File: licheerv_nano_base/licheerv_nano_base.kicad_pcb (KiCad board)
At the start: 2 copper layers, 186 x 50 mm, 112 parts, among them J1 USB STM32, J10 Valve, J11 ETH_IN, J12 ETH_OUT, J13 Compressor, J14 DebugUART, J15 Weight, J16 Malibotti, J17 Robot, J18 SWDBG, J19 IO, J2 Barrel_Jack_Switch, J3 TOF1, J4 TOF1, J5 TOF1, J6 TOF1, J7 STEP1, J8 STEP2, J9 Conveyor, Q1 BC807, Q2 IRLML6344, Q3 IRLML6344, Q4 IRLML6344, U1 TPS54202DDC, U2 STM32G431RBTx, U3 HX711, U5 TMC2209, U6 TMC2209

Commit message: Initial commit lichee_rv_nano_base pcb
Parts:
- added FID2: Fiducial, liebler_DRAWINGS:barrel_jack_positive_polarity, F.Cu at (155.9, 68.8)
- added R11: 10k, Resistor_SMD:R_0201_0603Metric, B.Cu at (168.2, 59.2)
- added U4: DCDC_MP2315, liebler_MODULES:DCDC_MP2315, F.Cu at (68.5, 77.8)
- C5, C7: footprint Capacitor_SMD:C_0603_1608Metric -> Capacitor_SMD:C_0805_2012Metric
- C8: value 1u -> 2u2
- J2: value Barrel_Jack_Switch -> DC IN
- J3: value TOF1 -> TOF3
- J4: value TOF1 -> TOF2
- L1: footprint liebler_PASSIVES:L_0630 -> Inductor_SMD:L_Abracon_ASPI-0630LR
- LS2: value Speaker_withoutTerminals -> Speaker
- Q1: footprint Package_TO_SOT_SMD:SOT-23_Handsoldering -> liebler_SEMICONDUCTORS:SOT-23_smaller
- R2: footprint Resistor_SMD:R_0201_0603Metric -> Resistor_SMD:R_0402_1005Metric
- R5, R6, R7: footprint Resistor_SMD:R_0805_2012Metric_Pad1.20x1.40mm_HandSolder -> Resistor_SMD:R_0402_1005Metric
- R8: value 20k -> 10k; footprint Resistor_SMD:R_0805_2012Metric_Pad1.20x1.40mm_HandSolder -> Resistor_SMD:R_0201_0603Metric
- TP1: value Stepper_UART -> StepperUART
- U7: value ~ -> PoE->24V
- moved J11 16.6 mm to (38.7, 64.6)
- moved C7 16.5 mm to (85.4, 73.0)
- moved J12 16.5 mm to (55.3, 64.6)
- moved C5 16.2 mm to (83.4, 73.0)
- moved J16 12.6 mm to (77.2, 91.9)
- moved J17 12.6 mm to (64.5, 91.9)
- moved L1 10.00 mm to (78.0, 69.2), turned to 180 degrees
- moved Q2 9.55 mm to (58.7, 61.5)
- moved R4 7.01 mm to (66.7, 66.6), turned to -90 degrees
- moved C3 6.80 mm to (67.9, 67.2), turned to 90 degrees
- moved R3 6.12 mm to (66.7, 68.3), turned to -90 degrees
- moved R2 6.03 mm to (67.2, 70.1), turned to 90 degrees
- moved L2 5.54 mm to (161.3, 57.0)
- moved C1 5.20 mm to (72.6, 71.9), turned to 180 degrees
- moved R7 4.95 mm to (168.8, 55.7)
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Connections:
- net Net-(J14-Pin_2) renamed /RX
- net Net-(J14-Pin_3) renamed /TX
- J3 pad 1: i1c -> i3c
- J3 pad 2: i1d -> i3d
- J3 pad 3: INT_TOF1 -> INT_TOF3
- J4 pad 1: i2c -> i1c
- J4 pad 2: i2d -> i1d
- J4 pad 3: INT_TOF2 -> INT_TOF1
- J5 pad 1: i3c -> i2c
- J5 pad 2: i3d -> i2d
- J5 pad 3: INT_TOF3 -> INT_TOF2
- R8 pad 2: Net-(U3-VFB) -> Net-(R11-Pad1)
- U2 pad 12: INT_TOF3 -> INT_TOF2
- U2 pad 13: INT_TOF2 -> INT_TOF1
- U2 pad 22: i2c -> i1c
- U2 pad 40: i3c -> i2c
- U2 pad 41: i3d -> i2d
- U2 pad 5: i2d -> i1d
- U2 pad 51: i1c -> i3c
- U2 pad 60: i1d -> i3d
- U2 pad 62: INT_TOF1 -> INT_TOF3
- U8 pad 23: MALIBOTTI_RXD -> ROBOT_RXD
- U8 pad 25: MALIBOTTI_TXD -> ROBOT_TXD
- U8 pad 27: ROBOT_RXD -> MALIBOTTI_RXD
- U8 pad 28: ROBOT_TXD -> MALIBOTTI_TXD
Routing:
- net +3V3: track 282.1 -> 341.9 mm, vias 9 -> 10
- net +5V: track 100.5 -> 83.6 mm, vias 1 -> 2
- net INT_TOF2: track 23.8 -> 6.99 mm
- net ROBOT_RXD: track 9.37 -> 25.9 mm
- net 5-24V: track 221.3 -> 236.7 mm, vias 9 -> 20
- net INT_TOF3: track 6.99 -> 21.8 mm
- net ROBOT_TXD: track 6.80 -> 21.1 mm
- net MALIBOTTI_RXD: track 24.0 -> 9.76 mm
- net GND: track 73.1 -> 86.8 mm, vias 12 -> 172
- net +9V: track 0.00 -> 12.2 mm
- net MALIBOTTI_TXD: track 19.3 -> 7.38 mm
- net INT_RGB: track 55.4 -> 43.5 mm, vias 0 -> 1
- net i2d: track 29.8 -> 20.2 mm
- net i1d: track 20.3 -> 29.8 mm
- net +48V: track 22.3 -> 14.8 mm
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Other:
- board text added: "+ -"
- board text added: "3V3"
- board text added: "5V"
- board text added: "9V"
- board text added: "A+"
- board text added: "A-"
- board text added: "A1"
- board text added: "A2"
- board text added: "B1"
- board text added: "B2"
- board text added: "Compr"
- board text added: "Conv"
- board text added: "E+"
- board text added: "E-"
- board text added: "GND"
- board text added: "I1C"
- board text added: "I1D"
- board text added: "I2C"
- board text added: "I2D"
- board text added: "I3C"
- board text added: "I3D"
- board text added: "IO1"
- board text added: "IO2"
- board text added: "IO3"
- board text added: "IO4"
- board text added: "IRQ"
- board text added: "IRQ1"
- board text added: "IRQ2"
- board text added: "IRQ3"
- board text added: "Malibotti"
- board text added: "RX"
- board text added: "RXD"
- board text added: "Robot"
- board text added: "SCL"
- board text added: "SDA"
- board text added: "Stepper1"
- board text added: "Stepper2"
- board text added: "TX"
- board text added: "TXD"
- board text added: "USB PD"
- board text added: "Valve"
- board text added: "Weightcell"

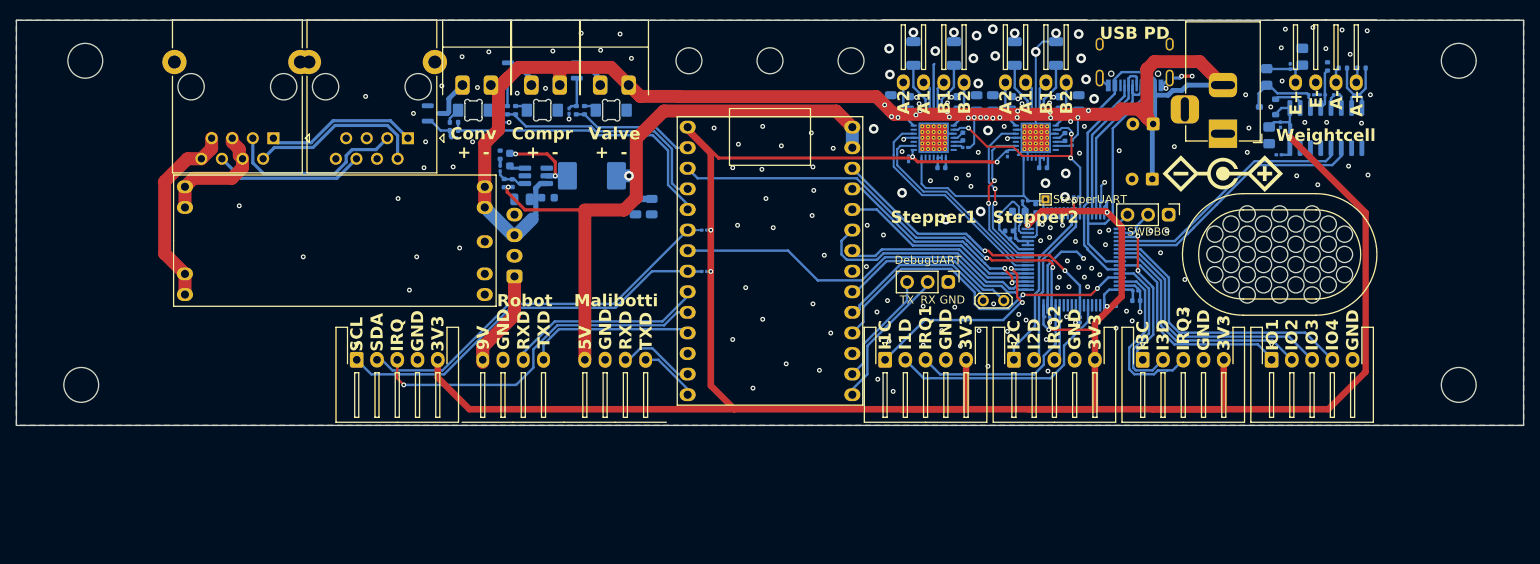
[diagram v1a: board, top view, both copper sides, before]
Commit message: lichee_rv_nano aka radxa zero 3e as ordered @ jlcpcb
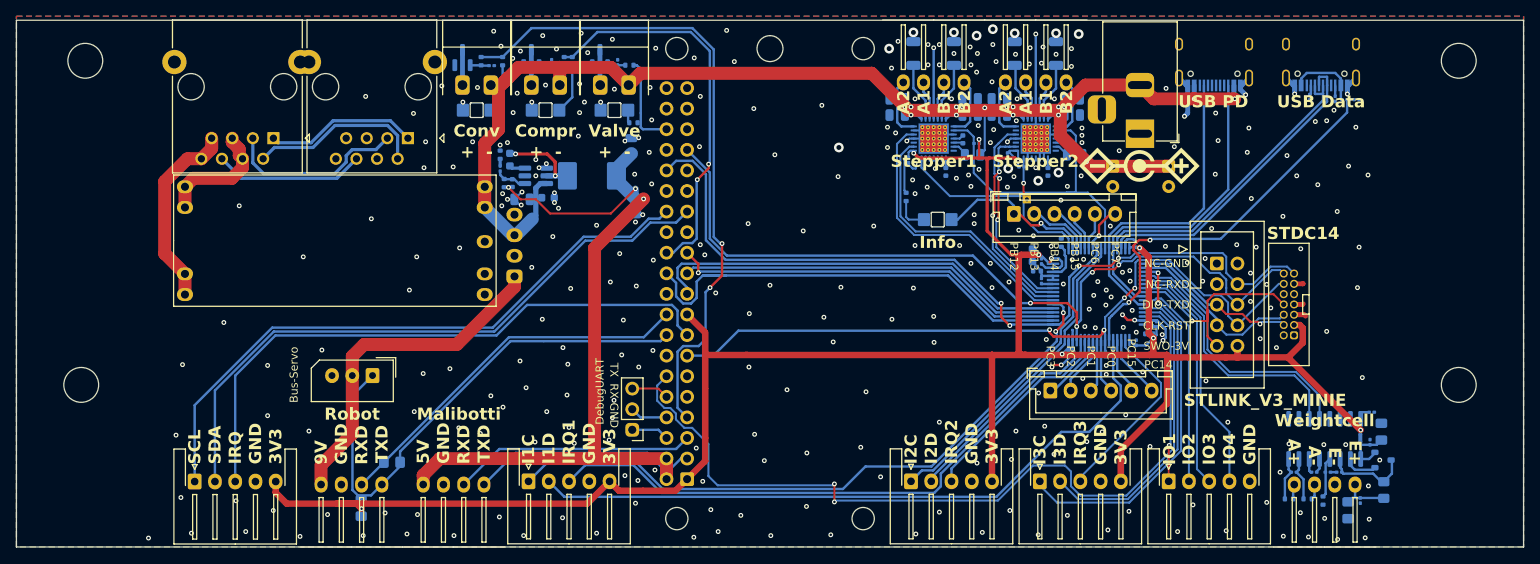
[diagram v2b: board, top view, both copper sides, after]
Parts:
- removed H5, H7: MountingHole, MountingHole:MountingHole_3.2mm_M3
- removed LS1: Speaker, TestPoint:TestPoint_2Pads_Pitch2.54mm_Drill0.8mm
- removed LS2: Speaker, liebler_MECH:SPEAKER_2415
- removed R12, R14: 4k7, Resistor_SMD:R_0201_0603Metric
- removed U8: ~, liebler_MODULES:LicheeRV_Nano
- added D4: Info, liebler_OPTO:LED_1206_3216Metric_ReverseMount, B.Cu at (120.7, 74.6)
- added J20: Bus-Servo, Connector_Molex:Molex_SPOX_5267-03A_1x03_P2.50mm_Vertical, F.Cu at (51.0, 93.8)
- added J21: STDC14, liebler_CONN:IDC_2x07_P1.27mm_Vertical, F.Cu at (164.0, 85.1)
- added J22: USB STM32, liebler_CONN:USB_C_Receptacle_HRO_TYPE-C-31-M-12_smaller, B.Cu at (168.0, 54.0)
- added J23: IO, Connector_JST:JST_XH_B6B-XH-A_1x06_P2.50mm_Vertical, F.Cu at (130.1, 73.9)
- added J24: IO, Connector_JST:JST_XH_B6B-XH-A_1x06_P2.50mm_Vertical, F.Cu at (134.6, 95.7)
- added R13: 5k1, Resistor_SMD:R_0201_0603Metric, B.Cu at (166.6, 59.5)
- added R28: 5k1, Resistor_SMD:R_0201_0603Metric, B.Cu at (169.8, 59.7)
- added R29: 10k, Resistor_SMD:R_0201_0603Metric, B.Cu at (170.9, 59.8)
- added R30: 10k, Resistor_SMD:R_0201_0603Metric, B.Cu at (172.4, 59.8)
- added R31: 1k, Resistor_SMD:R_0402_1005Metric, B.Cu at (116.8, 71.8)
- added R76: 10k, Resistor_SMD:R_0805_2012Metric_Pad1.20x1.40mm_HandSolder, B.Cu at (49.5, 110.2)
- added R77: 1k, Resistor_SMD:R_0805_2012Metric_Pad1.20x1.40mm_HandSolder, B.Cu at (53.4, 104.5)
- added X1: Radxa Zero 3E, liebler_MODULES:Radxa Zero 3E, B.Cu at (88.5, 82.5)
- C25, C26: footprint Capacitor_SMD:C_0201_0603Metric -> Capacitor_SMD:C_0805_2012Metric
- C29, C30, C42, C43: footprint Capacitor_SMD:C_0603_1608Metric -> Capacitor_SMD:C_0805_2012Metric
- J18: value SWDBG -> STLINK_V3_MINIE; footprint liebler_CONN:PinHeader_1x03_P2.54mm_Vertical_smallerCourtyard -> Connector_IDC:IDC-Header_2x05_P2.54mm_Vertical
- TP1: moved to B.Cu
- moved C10 56.3 mm to (171.3, 110.5), turned to -90 degrees
- moved C6 54.3 mm to (172.8, 109.3), turned to -90 degrees
- moved R5 53.9 mm to (164.1, 109.1), turned to 0 degrees
- moved R7 53.6 mm to (168.2, 109.3), turned to -90 degrees
- moved R6 53.4 mm to (166.3, 109.1), turned to 0 degrees
- moved L2 53.0 mm to (175.8, 108.0), turned to 90 degrees
- moved J15 50.2 mm to (164.7, 107.3), turned to 0 degrees
- moved C11 47.2 mm to (164.7, 105.8), turned to 0 degrees
- moved R8 46.7 mm to (170.2, 105.8), turned to 180 degrees
- moved C13 46.7 mm to (167.2, 105.8), turned to 0 degrees
- moved R11 46.6 mm to (168.8, 105.8), turned to 180 degrees
- moved J4 46.5 mm to (70.2, 106.9)
- moved Q1 45.8 mm to (175.7, 104.3), turned to 0 degrees
- moved J14 43.1 mm to (83.0, 100.5), turned to 180 degrees
- moved C20 40.7 mm to (174.1, 102.1), turned to 90 degrees
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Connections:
- net /BOOT renamed /psu/BOOT
- net /FB renamed /psu/FB
- net /SW renamed /psu/SW
- J1 pad A6: USBPD_D+ -> unconnected-(J1-D+-PadA6)
- J1 pad A7: USBPD_D- -> unconnected-(J1-D--PadA7)
- J1 pad B6: USBPD_D+ -> unconnected-(J1-D+-PadB6)
- J1 pad B7: USBPD_D- -> unconnected-(J1-D--PadB7)
- J18 pad 1: GND -> unconnected-(J18-Pin_1-Pad1)
- J18 pad 2: SWCLK -> GND
- J18 pad 3: SWDIO -> unconnected-(J18-Pin_3-Pad3)
- U2 pad 2: unconnected-(U2-PC13-Pad2) -> INT_TOF3
- U2 pad 3: unconnected-(U2-PC14-Pad3) -> PC14
- U2 pad 4: unconnected-(U2-PC15-Pad4) -> PC15
- U2 pad 56: IO2 -> SWO
- U2 pad 58: IO1 -> IO2
- U2 pad 6: unconnected-(U2-PF1-Pad6) -> USB_VSENSE
- U2 pad 62: INT_TOF3 -> IO1
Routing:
- net STM32_BOOT: track 42.1 -> 103.0 mm
- net 5-24V: track 236.7 -> 177.1 mm, vias 20 -> 16
- net STM32BOOT_RXD: track 46.6 -> 102.7 mm, vias 0 -> 4
- net i1c: track 26.8 -> 81.7 mm
- net i1d: track 29.8 -> 84.1 mm
- net STM32_RESET: track 38.0 -> 91.2 mm, vias 2 -> 4
- net INT_TOF1: track 23.8 -> 75.0 mm
- net USB_VSENSE: track 0.00 -> 49.4 mm, vias 0 -> 2
- net STM32BOOT_TXD: track 55.1 -> 102.0 mm, vias 2 -> 4
- net +3V3: track 341.9 -> 295.6 mm, vias 10 -> 9
- net Conveyor_PWM: track 36.2 -> 81.1 mm, vias 0 -> 2
- net ROBOT_TXD: track 21.1 -> 63.4 mm
- net INT_RGB: track 43.5 -> 75.1 mm, vias 1 -> 0
- net SDA: track 47.8 -> 78.7 mm
- net +9V: track 12.2 -> 42.3 mm
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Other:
- board size 186 x 50 mm -> 186 x 65 mm
- board text added: "CLK-RST"
- board text added: "DIO-TXD"
- board text added: "Info"
- board text added: "NC-GND"
- board text added: "NC-RXD"
- board text added: "PB12"
- board text added: "PB13"
- board text added: "PB14"
- board text added: "PB15"
- board text added: "PC0"
- board text added: "PC1"
- board text added: "PC14"
- board text added: "PC15"
- board text added: "PC2"
- board text added: "PC3"
- board text added: "PC6"
- board text added: "PC7"
- board text added: "STDC14"
- board text added: "SWO-3V"
- board text added: "USB Data"
